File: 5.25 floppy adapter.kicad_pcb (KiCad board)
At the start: 2 copper layers, 48.3 x 26 mm, 2 parts

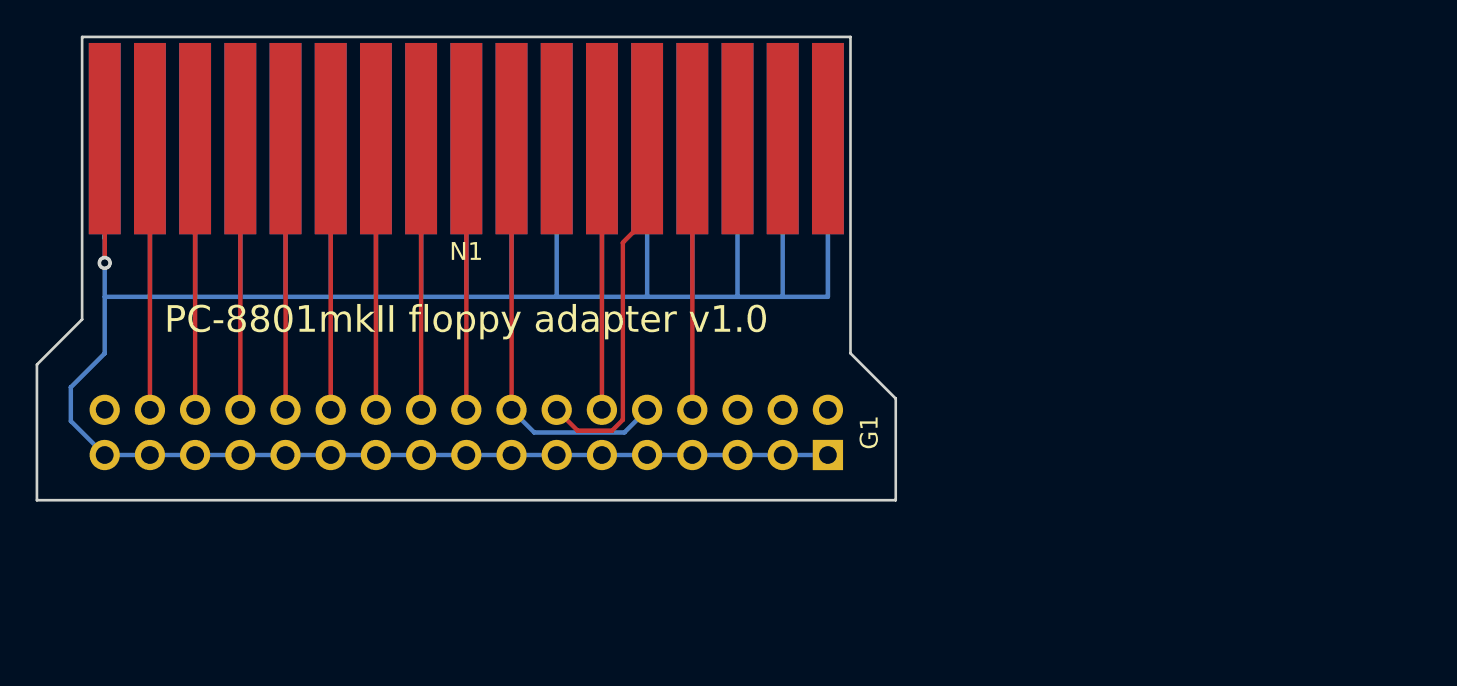
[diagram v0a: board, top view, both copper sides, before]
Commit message: added an actual IDC connector and flipped the board around so it will actually work this time
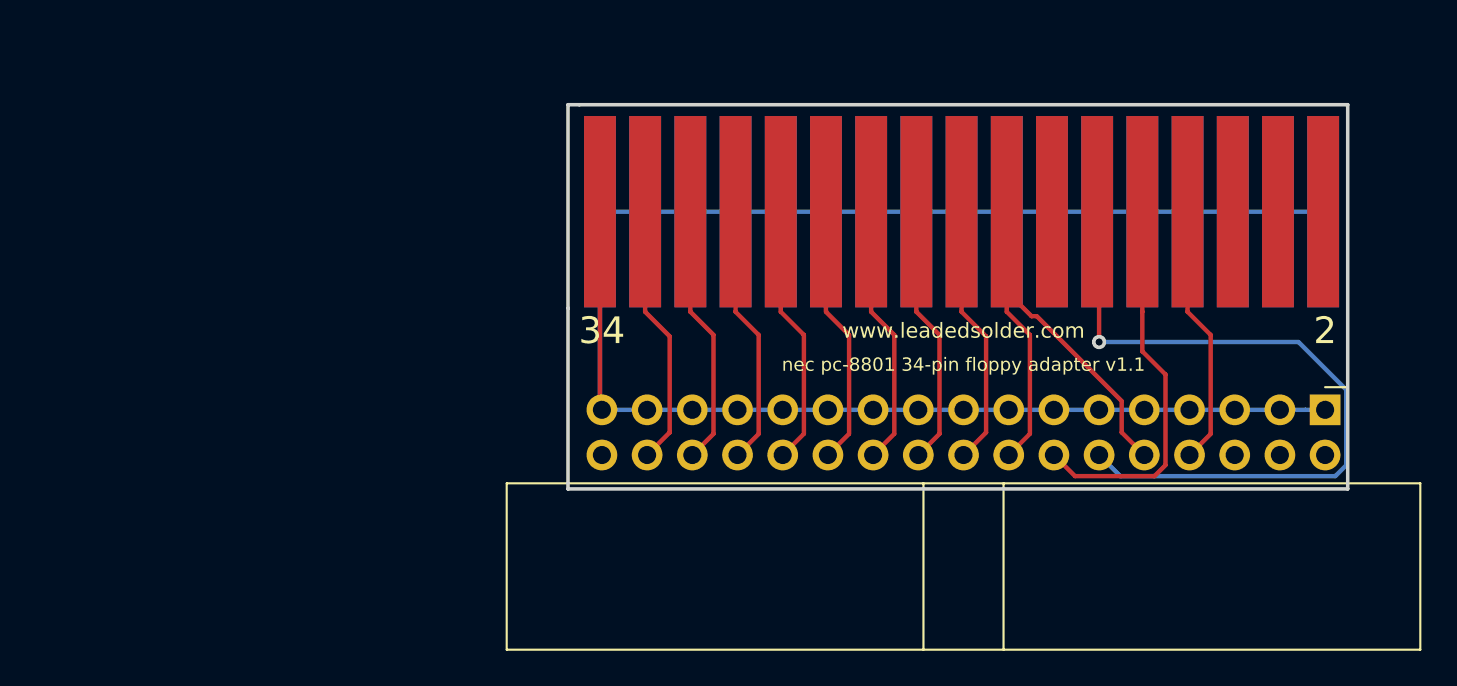
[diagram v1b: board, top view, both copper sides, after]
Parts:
- G1: footprint Pin_Headers:Pin_Header_Straight_2x17_Pitch2.54mm -> Connector_IDC:IDC-Header_2x17_P2.54mm_Horizontal; moved to F.Cu
- moved N1 28.1 mm to (177.7, 86.7)
- moved G1 28.1 mm to (198.1, 95.2), turned to 270 degrees
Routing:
- net GND: track 255.5 -> 103.6 mm, vias 1 -> 0
- net Net-(G1-Pad12): track 15.2 -> 41.2 mm, vias 0 -> 1
- net Net-(G1-Pad10): track 23.9 -> 31.8 mm
- net Net-(G1-Pad14): track 20.8 -> 21.8 mm
- net Net-(G1-Pad28): track 15.2 -> 14.7 mm
- net Net-(G1-Pad26): track 15.2 -> 14.7 mm
- net Net-(G1-Pad22): track 15.2 -> 14.7 mm
- net Net-(G1-Pad20): track 15.2 -> 14.7 mm
- net Net-(G1-Pad8): track 15.2 -> 14.7 mm
- net Net-(G1-Pad30): track 15.2 -> 14.7 mm
- net Net-(G1-Pad24): track 15.2 -> 14.7 mm
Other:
- board size 48.3 x 26 mm -> 43.8 x 21.6 mm
- board text added: "2"
- board text added: "34"
- board text added: "nec pc-8801 34-pin floppy adapter v1.1"
- board text removed: "PC-8801mkII floppy adapter v1.0"
- board text removed: "THIS SIDE DOWN"

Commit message: More silkscreen
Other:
- board text added: "1"
- board text added: "33"
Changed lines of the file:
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@@
   (general
     (thickness 1.6)
-    (drawings 10)
+    (drawings 12)
     (tracks 70)
     (zones 0)
@@
       (net 17 GND) (clearance 0.375))
   )
+  (gr_text 33 (at 157.48 90.805) (layer B.SilkS)
+    (effects (font (size 1.5 1.5) (thickness 0.3)) (justify mirror))
+  )
+  (gr_text 1 (at 198.12 90.805) (layer B.SilkS)
+    (effects (font (size 1.5 1.5) (thickness 0.3)) (justify mirror))
+  )
   (gr_text 34 (at 157.48 90.805) (layer F.SilkS)

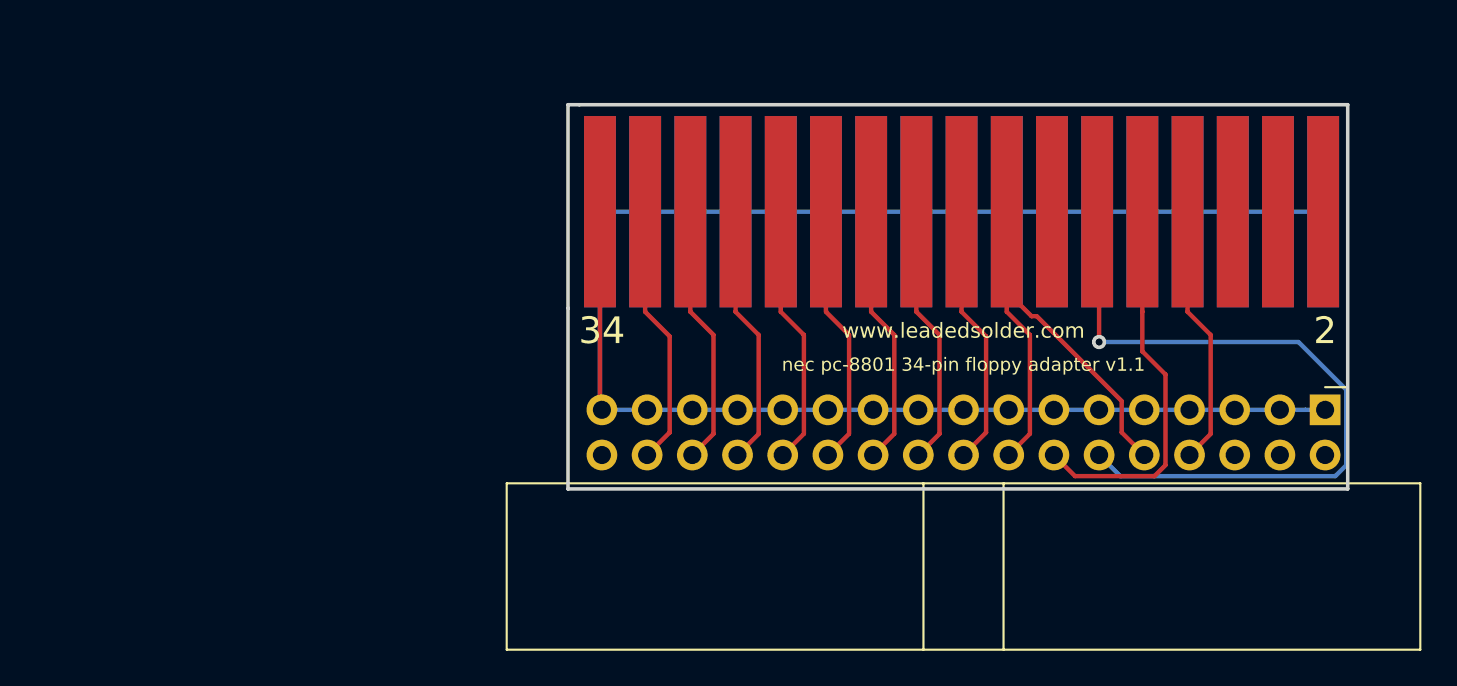
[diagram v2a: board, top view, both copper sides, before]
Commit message: Adding a little more meat around the fingers so it will mount straighter, might still need to tweak
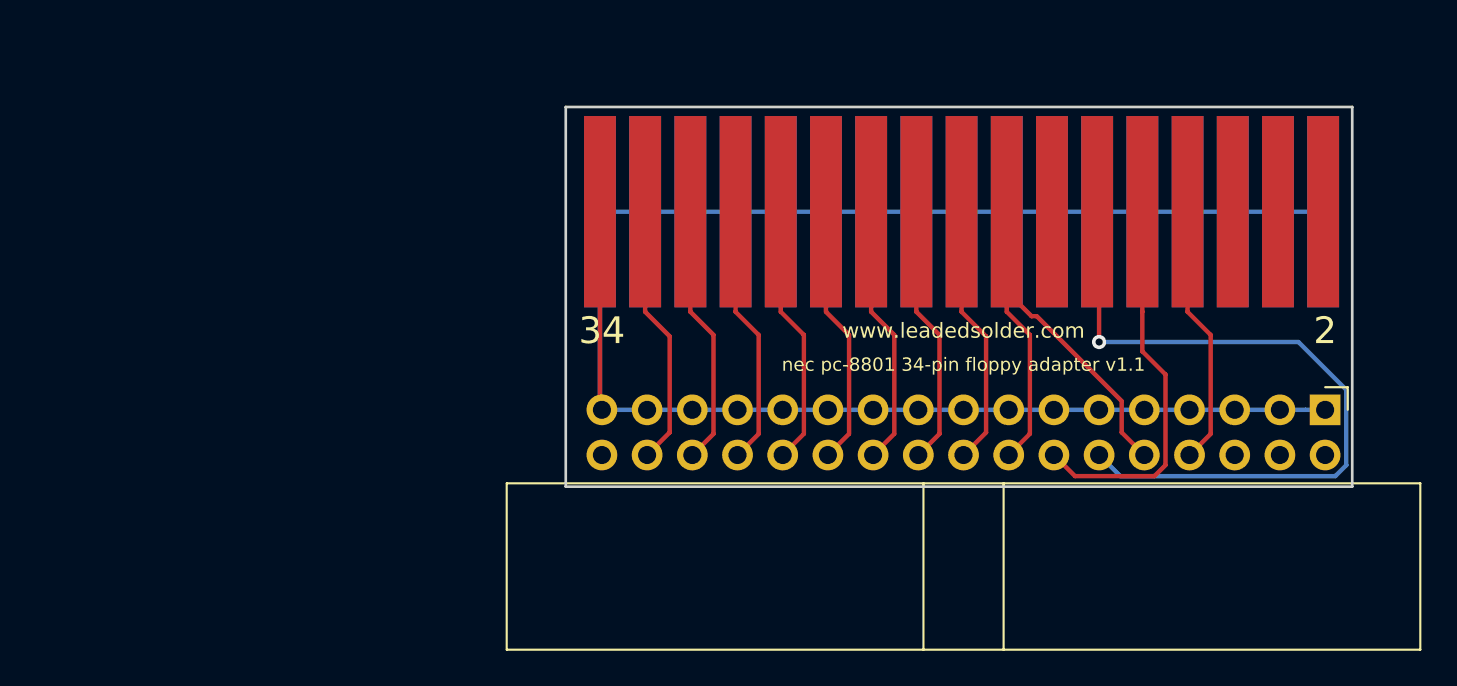
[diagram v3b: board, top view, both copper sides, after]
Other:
- board size 43.8 x 21.6 mm -> 44.2 x 21.3 mm
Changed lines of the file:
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@@
   (general
     (thickness 1.6)
-    (drawings 12)
+    (drawings 10)
     (tracks 70)
     (zones 0)
@@
       (net 17 GND) (clearance 0.375))
   )
+  (gr_line (start 155.448 99.568) (end 155.448 78.232) (layer Edge.Cuts) (width 0.15))
+  (gr_line (start 199.644 78.232) (end 199.644 99.568) (layer Edge.Cuts) (width 0.15))
+  (gr_line (start 199.644 99.568) (end 155.448 99.568) (layer Edge.Cuts) (width 0.15))
+  (gr_line (start 199.644 78.232) (end 155.448 78.232) (layer Edge.Cuts) (width 0.15))
   (gr_text 33 (at 157.48 90.805) (layer B.SilkS)
     (effects (font (size 1.5 1.5) (thickness 0.3)) (justify mirror))
@@
     (effects (font (size 0.75 0.75) (thickness 0.1875)))
   )
-  (gr_line (start 199.39 99.695) (end 199.39 78.105) (layer Edge.Cuts) (width 0.2))
-  (gr_line (start 155.575 99.695) (end 199.39 99.695) (layer Edge.Cuts) (width 0.2))
-  (gr_line (start 155.575 89.535) (end 155.575 99.695) (layer Edge.Cuts) (width 0.2))
-  (gr_line (start 155.575 78.105) (end 155.575 89.535) (layer Edge.Cuts) (width 0.2))
-  (gr_line (start 156.21 78.105) (end 155.575 78.105) (layer Edge.Cuts) (width 0.2))
-  (gr_line (start 199.39 78.105) (end 156.21 78.105) (layer Edge.Cuts) (width 0.2))
   (segment (start 190.39 89.74) (end 190.39 84.115) (width 0.25) (layer F.Cu) (net 4))
   (segment (start 191.688601 91.038601) (end 190.39 89.74) (width 0.25) (layer F.Cu) (net 4))

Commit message: Straight-through version
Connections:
- G1 pad 16: Net-(G1-Pad10) -> Net-(G1-Pad16)
- N1 pad 10: Net-(G1-Pad14) -> Net-(G1-Pad10)
- N1 pad 14: Net-(N1-Pad14) -> Net-(G1-Pad14)
- N1 pad 16: Net-(G1-Pad10) -> Net-(G1-Pad16)
- N1 pad 2: Net-(N1-Pad2) -> Net-(G1-Pad2)
- N1 pad 34: GND -> Net-(G1-Pad34)
- N1 pad 4: Net-(N1-Pad4) -> Net-(G1-Pad4)
- N1 pad 6: Net-(N1-Pad6) -> Net-(G1-Pad6)
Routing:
- net Net-(G1-Pad12): track 41.2 -> 14.7 mm, vias 1 -> 0
- net Net-(G1-Pad6): track 0.00 -> 20.2 mm
- net Net-(G1-Pad2): track 0.00 -> 19.8 mm
- net Net-(G1-Pad4): track 0.00 -> 19.8 mm
- net Net-(G1-Pad16): track 0.00 -> 14.7 mm
- net Net-(G1-Pad34): track 0.00 -> 14.7 mm
- net Net-(G1-Pad10): track 31.8 -> 20.2 mm
- net GND: track 103.6 -> 92.5 mm
- net Net-(G1-Pad14): track 21.8 -> 14.7 mm
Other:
- board text added: "DS0"
- board text added: "DS1"
- board text added: "DS2"
- board text added: "DS3"
- board text added: "IDX"
- board text added: "nec pc-8801 34-pin floppy adapter v2.0"
- board text removed: "nec pc-8801 34-pin floppy adapter v1.1"

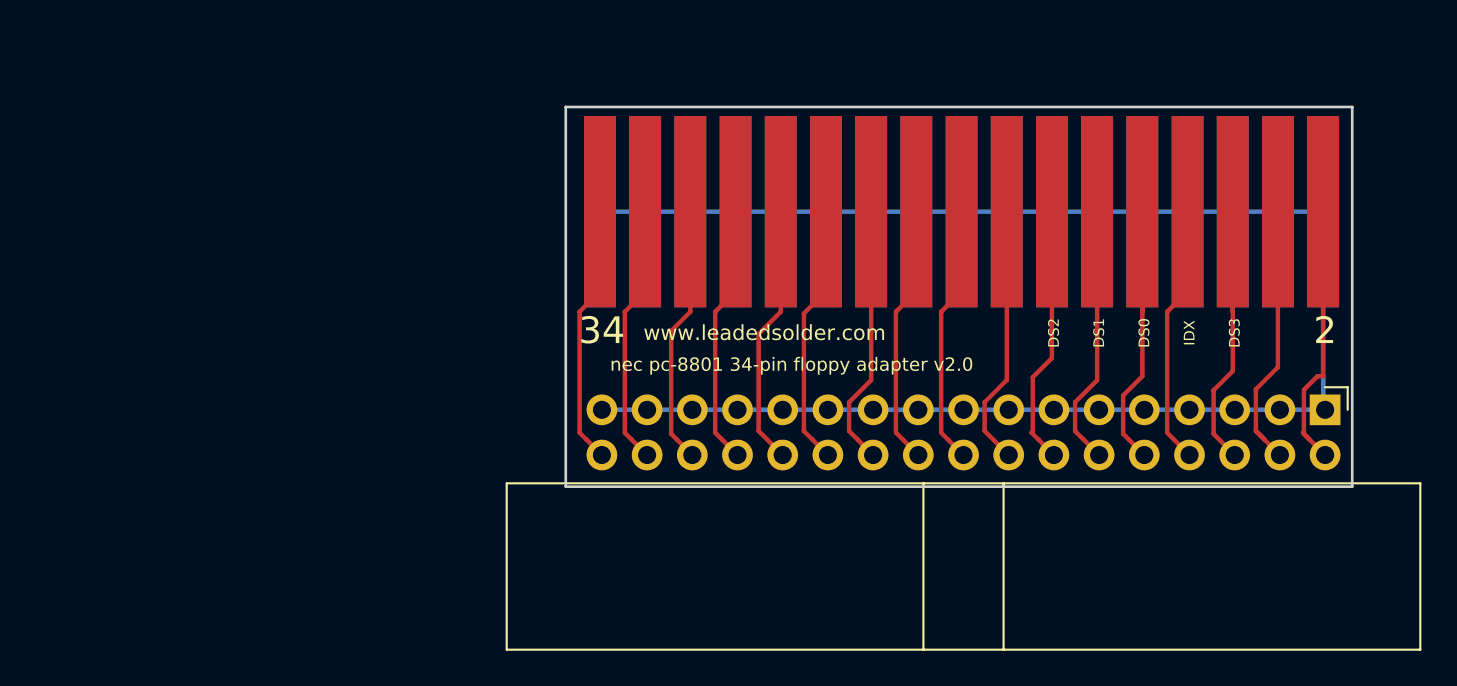
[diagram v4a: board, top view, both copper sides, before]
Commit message: Solder mask area, ground plane
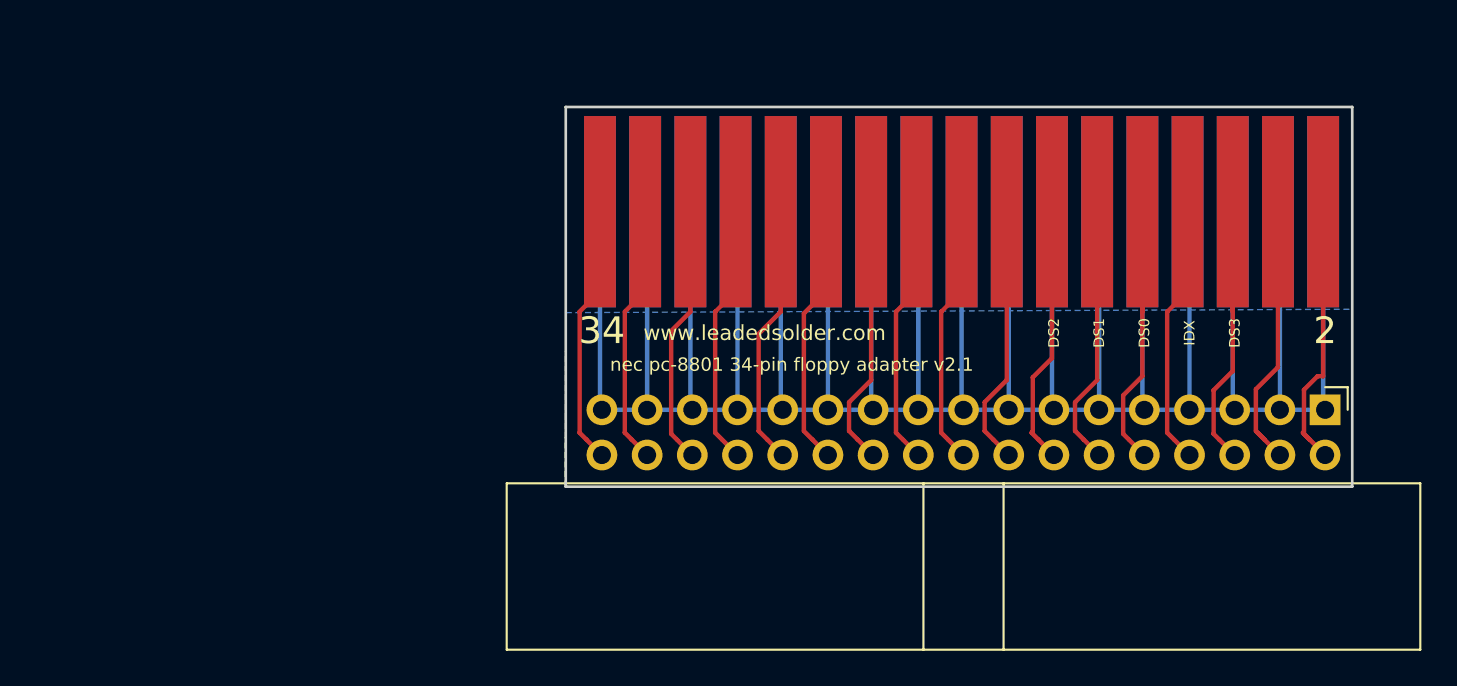
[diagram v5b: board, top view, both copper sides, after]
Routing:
- net GND: track 92.5 -> 230.7 mm
- added copper zone on B.Cu, net GND
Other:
- board text added: "nec pc-8801 34-pin floppy adapter v2.1"
- board text removed: "nec pc-8801 34-pin floppy adapter v2.0"
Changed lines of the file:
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@@
-(kicad_pcb (version 20171130) (host pcbnew "(5.0.0-3-g5ebb6b6)")
+(kicad_pcb (version 20171130) (host pcbnew "(5.1.4-0-10_14)")
   (general
     (thickness 1.6)
     (drawings 15)
-    (tracks 97)
+    (tracks 128)
     (zones 0)
     (modules 2)
@@
     (zone_45_only no)
     (trace_min 0.2)
-    (segment_width 0.2)
-    (edge_width 0.15)
     (via_size 0.8)
     (via_drill 0.4)
@@
     (uvia_min_size 0.2)
     (uvia_min_drill 0.1)
+    (edge_width 0.15)
+    (segment_width 0.2)
     (pcb_text_width 0.3)
     (pcb_text_size 1.5 1.5)
@@
     (effects (font (size 0.85 0.85) (thickness 0.2125)))
   )
-  (gr_text "nec pc-8801 34-pin floppy adapter v2.0" (at 168.148 92.71) (layer F.SilkS)
+  (gr_text "nec pc-8801 34-pin floppy adapter v2.1" (at 168.148 92.71) (layer F.SilkS)
     (effects (font (size 0.75 0.75) (thickness 0.1875)))
   )
@@
   (segment (start 159.91 88.595) (end 158.765 89.74) (width 0.25) (layer F.Cu) (net 12))
   (segment (start 159.91 84.115) (end 159.91 88.595) (width 0.25) (layer F.Cu) (net 12))
-  (segment (start 157.37 84.115) (end 198.01 84.115) (width 0.25) (layer B.Cu) (net 13))
   (segment (start 198.01 95.14) (end 198.12 95.25) (width 0.25) (layer B.Cu) (net 13))
   (segment (start 198.01 84.115) (end 198.01 95.14) (width 0.25) (layer B.Cu) (net 13))
   (segment (start 198.12 95.25) (end 157.48 95.25) (width 0.25) (layer B.Cu) (net 13))
+  (segment (start 195.58 84.225) (end 195.47 84.115) (width 0.25) (layer B.Cu) (net 13))
+  (segment (start 195.58 95.25) (end 195.58 84.225) (width 0.25) (layer B.Cu) (net 13))
+  (segment (start 192.93 95.14) (end 193.04 95.25) (width 0.25) (layer B.Cu) (net 13))
+  (segment (start 192.93 84.115) (end 192.93 95.14) (width 0.25) (layer B.Cu) (net 13))
+  (segment (start 190.5 84.225) (end 190.39 84.115) (width 0.25) (layer B.Cu) (net 13))
+  (segment (start 190.5 95.25) (end 190.5 84.225) (width 0.25) (layer B.Cu) (net 13))
+  (segment (start 187.85 95.14) (end 187.96 95.25) (width 0.25) (layer B.Cu) (net 13))
+  (segment (start 187.85 84.115) (end 187.85 95.14) (width 0.25) (layer B.Cu) (net 13))
+  (segment (start 185.42 84.225) (end 185.31 84.115) (width 0.25) (layer B.Cu) (net 13))
+  (segment (start 185.42 95.25) (end 185.42 84.225) (width 0.25) (layer B.Cu) (net 13))
+  (segment (start 182.77 95.14) (end 182.88 95.25) (width 0.25) (layer B.Cu) (net 13))
+  (segment (start 182.77 84.115) (end 182.77 95.14) (width 0.25) (layer B.Cu) (net 13))
+  (segment (start 180.34 84.225) (end 180.23 84.115) (width 0.25) (layer B.Cu) (net 13))
+  (segment (start 180.34 95.25) (end 180.34 84.225) (width 0.25) (layer B.Cu) (net 13))
+  (segment (start 177.69 95.14) (end 177.8 95.25) (width 0.25) (layer B.Cu) (net 13))
+  (segment (start 177.69 84.115) (end 177.69 95.14) (width 0.25) (layer B.Cu) (net 13))
+  (segment (start 175.26 84.225) (end 175.15 84.115) (width 0.25) (layer B.Cu) (net 13))
+  (segment (start 175.26 95.25) (end 175.26 84.225) (width 0.25) (layer B.Cu) (net 13))
+  (segment (start 172.61 95.14) (end 172.72 95.25) (width 0.25) (layer B.Cu) (net 13))
+  (segment (start 172.61 84.115) (end 172.61 95.14) (width 0.25) (layer B.Cu) (net 13))
+  (segment (start 170.18 84.225) (end 170.07 84.115) (width 0.25) (layer B.Cu) (net 13))
+  (segment (start 170.18 95.25) (end 170.18 84.225) (width 0.25) (layer B.Cu) (net 13))
+  (segment (start 167.53 95.14) (end 167.64 95.25) (width 0.25) (layer B.Cu) (net 13))
+  (segment (start 167.53 84.115) (end 167.53 95.14) (width 0.25) (layer B.Cu) (net 13))
+  (segment (start 165.1 84.225) (end 164.99 84.115) (width 0.25) (layer B.Cu) (net 13))
+  (segment (start 165.1 95.25) (end 165.1 84.225) (width 0.25) (layer B.Cu) (net 13))
+  (segment (start 162.45 95.14) (end 162.56 95.25) (width 0.25) (layer B.Cu) (net 13))
+  (segment (start 162.45 84.115) (end 162.45 95.14) (width 0.25) (layer B.Cu) (net 13))
+  (segment (start 160.02 84.225) (end 159.91 84.115) (width 0.25) (layer B.Cu) (net 13))
+  (segment (start 160.02 95.25) (end 160.02 84.225) (width 0.25) (layer B.Cu) (net 13))
+  (segment (start 157.37 95.14) (end 157.48 95.25) (width 0.25) (layer B.Cu) (net 13))
+  (segment (start 157.37 84.115) (end 157.37 95.14) (width 0.25) (layer B.Cu) (net 13))
   (segment (start 196.865 96.535) (end 197.256401 96.926401) (width 0.25) (layer F.Cu) (net 14))
   (segment (start 198.01 84.115) (end 198.01 88.595) (width 0.25) (layer F.Cu) (net 14))
@@
   (segment (start 180.23 93.582) (end 178.988601 94.823399) (width 0.25) (layer F.Cu) (net 18))
   (segment (start 180.23 84.115) (end 180.23 93.582) (width 0.25) (layer F.Cu) (net 18))
+  (zone (net 0) (net_name "") (layer F.Mask) (hatch edge 0.508)
+    (connect_pads (clearance 0.508))
+    (min_thickness 0.254)
+    (fill yes (arc_segments 32) (thermal_gap 0.508) (thermal_bridge_width 0.508))
+    (polygon
+      (pts
+        (xy 199.644 89.408) (xy 155.3845 89.408) (xy 155.448 78.2955) (xy 199.644 78.232)
+      )
+    )
+  )
+  (zone (net 0) (net_name "") (layer B.Mask) (hatch edge 0.508)
+    (connect_pads (clearance 0.508))
+    (min_thickness 0.254)
+    (fill yes (arc_segments 32) (thermal_gap 0.508) (thermal_bridge_width 0.508))
+    (polygon
+      (pts
+        (xy 199.644 89.4715) (xy 155.448 89.4715) (xy 155.448 78.2955) (xy 199.5805 78.232)
+      )
+    )
+  )
+  (zone (net 13) (net_name GND) (layer B.Cu) (hatch edge 0.508)
+    (connect_pads (clearance 0.508))
+    (min_thickness 0.254)
+    (fill yes (arc_segments 32) (thermal_gap 0.508) (thermal_bridge_width 0.508))
+    (polygon
+      (pts
+        (xy 199.644 89.5985) (xy 199.644 99.568) (xy 155.3845 99.568) (xy 155.448 89.789)
+      )
+    )
+  )
 )
